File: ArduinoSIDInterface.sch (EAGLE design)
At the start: 25 parts, among them IC1 74HC595N, IC2 74HC595N, T1 BC547

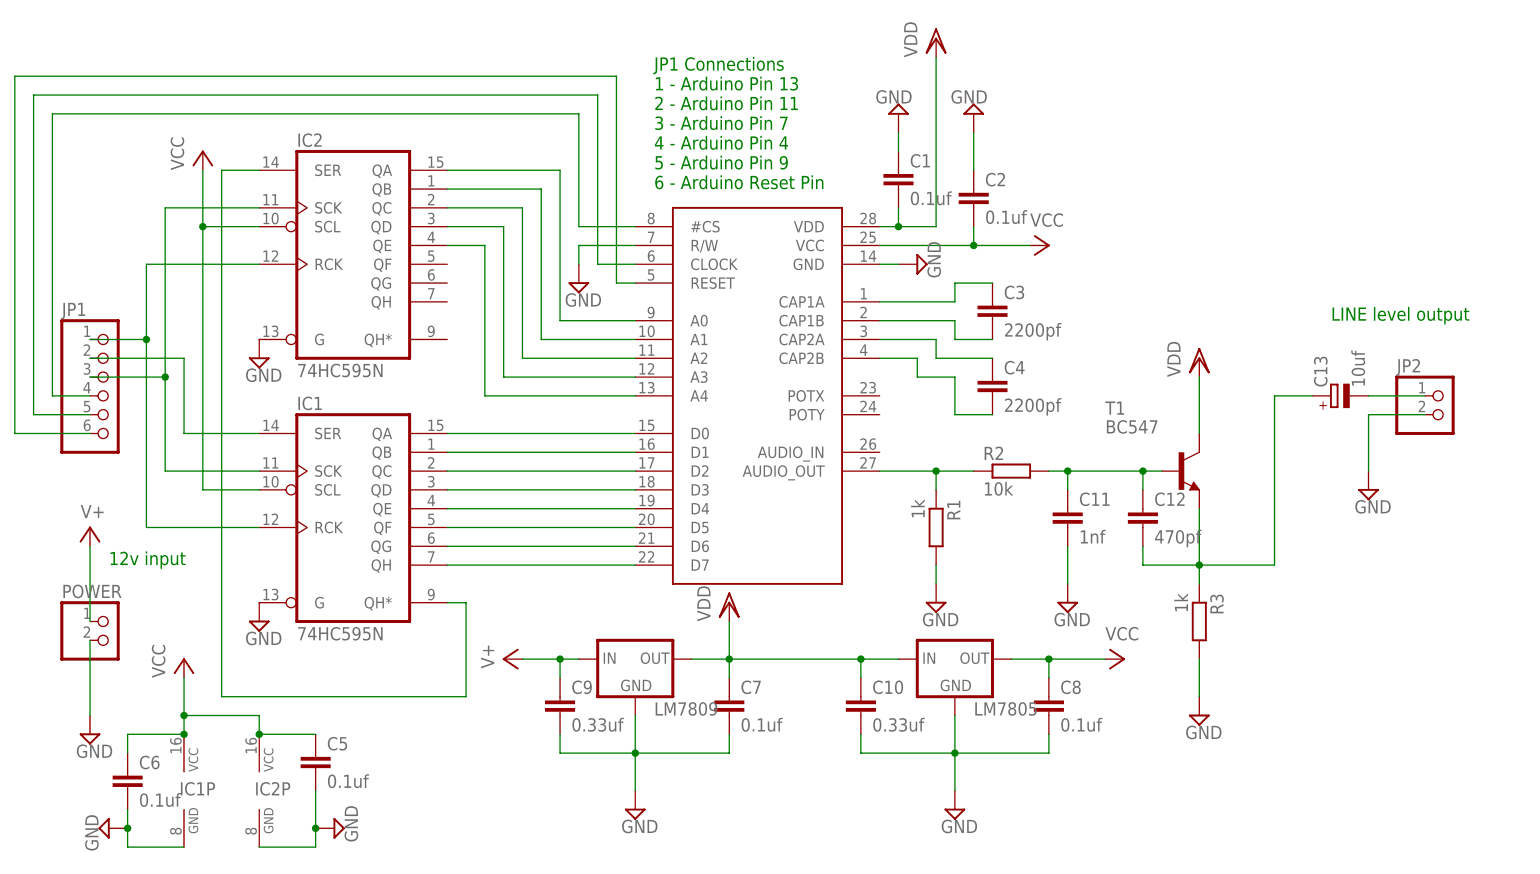
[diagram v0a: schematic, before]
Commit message: Revised the schematic and board layout. Shift register->SID connections now inverted so Q7->D0 and Q0->D7. Requires a change to the SPI initialisation to be compatible but the board layout is a lot neater. Now only a single layer, no extra wires required. Make the power lines a lot thicker - I believe this is the thing to do. Added additional 5v power out header to power external Arduino.
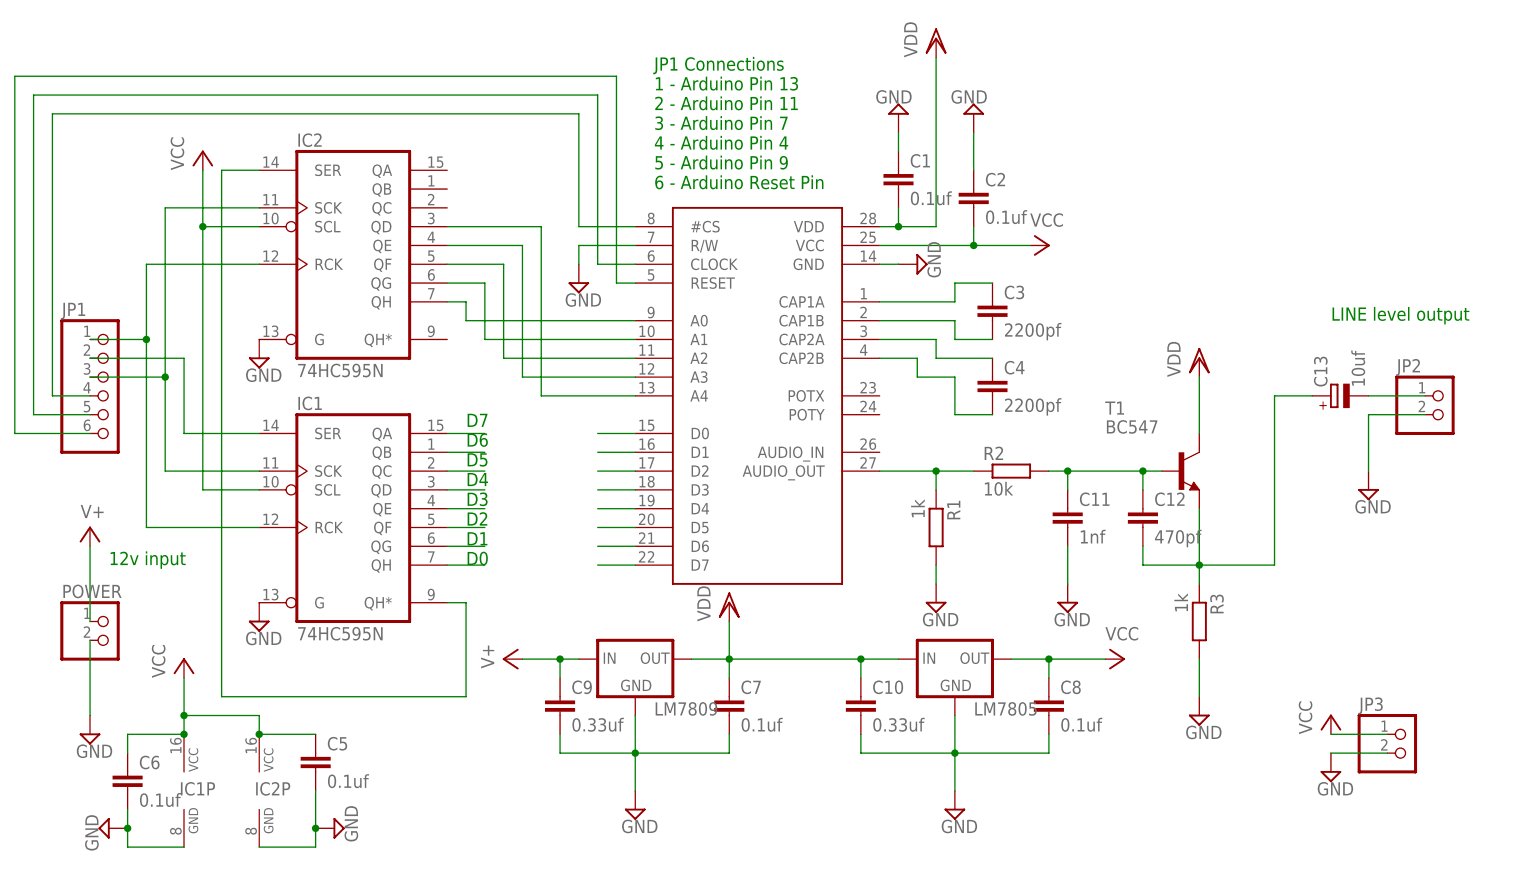
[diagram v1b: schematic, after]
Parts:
- added JP3: (no value), pinhead:PINHD-1X2
- C1: device rcl:C-EU025-030X050 -> rcl:C-EU050-035X075
- C2: device rcl:C-EU025-030X050 -> rcl:C-EU050-030X075
- C3, C4: device rcl:C-EU050-075X075 -> rcl:C-EU075-042X103
- C5, C6: device rcl:C-EU025-025X050 -> rcl:C-EU050-030X075
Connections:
- removed net N$10: IC1A.QB, U$1.D1
- removed net N$13: IC1A.QE, U$1.D4
- removed net N$14: IC1A.QC, U$1.D2
- removed net N$15: IC1A.QD, U$1.D3
- removed net N$18: IC1A.QG, U$1.D6
- removed net N$19: IC1A.QH, U$1.D7
- removed net N$8: IC1A.QF, U$1.D5
- removed net N$9: IC1A.QA, U$1.D0
- new net D0: IC1A.QH, U$1.D0
- new net D1: IC1A.QG, U$1.D1
- new net D2: IC1A.QF, U$1.D2
- new net D3: IC1A.QE, U$1.D3
- new net D4: IC1A.QD, U$1.D4
- new net D5: IC1A.QC, U$1.D5
- new net D6: IC1A.QB, U$1.D6
- new net D7: IC1A.QA, U$1.D7
- net GND: now also JP3.2
- net N$3: now also IC2A.QH; no longer IC2A.QA
- net N$4: now also IC2A.QG; no longer IC2A.QB
- net N$5: now also IC2A.QF; no longer IC2A.QC
- net N$6: now also IC2A.QE; no longer IC2A.QD
- net N$7: now also IC2A.QD; no longer IC2A.QE
- net VCC: now also JP3.1
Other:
- note added: "D7 D6 D5 D4 D3 D2 D1 D0"

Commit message: Fixup schematic
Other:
- note removed: "D7 D6 D5 D4 D3 D2 D1 D0"
- moved on the sheet: IC1
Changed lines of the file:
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@@
 <text x="-25.4" y="27.94" size="1.778" layer="91">12v input</text>
 <text x="139.7" y="60.96" size="1.778" layer="91">LINE level output</text>
-<text x="22.86" y="27.94" size="1.778" layer="91">D7
-D6
-D5
-D4
-D3
-D2
-D1
-D0</text>
 </plain>
 <instances>
 <instance part="U$1" gate="G$1" x="73.66" y="48.26"/>
-<instance part="IC1" gate="A" x="7.62" y="35.56"/>
+<instance part="IC1" gate="A" x="7.62" y="35.56" rot="MR180"/>
 <instance part="IC2" gate="A" x="7.62" y="71.12" smashed="yes">
 <attribute name="NAME" x="0" y="84.455" size="1.778" layer="95" font="vector"/>
@@
 <instance part="C1" gate="G$1" x="81.28" y="81.28"/>
 <instance part="C2" gate="G$1" x="91.44" y="78.74"/>
-<instance part="SUPPLY3" gate="GND" x="-5.08" y="20.32"/>
+<instance part="SUPPLY3" gate="GND" x="-5.08" y="43.18"/>
 <instance part="SUPPLY4" gate="GND" x="-5.08" y="55.88"/>
 <instance part="SUPPLY5" gate="GND" x="81.28" y="88.9" rot="R180"/>
@@
 <segment>
 <pinref part="IC1" gate="A" pin="QH*"/>
-<wire x1="20.32" y1="22.86" x2="22.86" y2="22.86" width="0.1524" layer="91"/>
-<wire x1="22.86" y1="22.86" x2="22.86" y2="10.16" width="0.1524" layer="91"/>
+<wire x1="20.32" y1="48.26" x2="22.86" y2="48.26" width="0.1524" layer="91"/>
+<wire x1="22.86" y1="48.26" x2="22.86" y2="10.16" width="0.1524" layer="91"/>
 <wire x1="22.86" y1="10.16" x2="-10.16" y2="10.16" width="0.1524" layer="91"/>
 <wire x1="-10.16" y1="10.16" x2="-10.16" y2="81.28" width="0.1524" layer="91"/>
@@
 <segment>
 <pinref part="IC1" gate="A" pin="SCK"/>
-<wire x1="-17.78" y1="40.64" x2="-5.08" y2="40.64" width="0.1524" layer="91"/>
+<wire x1="-17.78" y1="30.48" x2="-5.08" y2="30.48" width="0.1524" layer="91"/>
 <pinref part="IC2" gate="A" pin="SCK"/>
-<wire x1="-17.78" y1="40.64" x2="-17.78" y2="53.34" width="0.1524" layer="91"/>
+<wire x1="-17.78" y1="30.48" x2="-17.78" y2="53.34" width="0.1524" layer="91"/>
 <wire x1="-17.78" y1="53.34" x2="-17.78" y2="76.2" width="0.1524" layer="91"/>
 <wire x1="-17.78" y1="76.2" x2="-5.08" y2="76.2" width="0.1524" layer="91"/>
@@
 <wire x1="-20.32" y1="68.58" x2="-5.08" y2="68.58" width="0.1524" layer="91"/>
 <pinref part="IC1" gate="A" pin="RCK"/>
-<wire x1="-5.08" y1="33.02" x2="-20.32" y2="33.02" width="0.1524" layer="91"/>
+<wire x1="-5.08" y1="38.1" x2="-20.32" y2="38.1" width="0.1524" layer="91"/>
 <wire x1="-20.32" y1="68.58" x2="-20.32" y2="58.42" width="0.1524" layer="91"/>
 <pinref part="JP1" gate="A" pin="1"/>
-<wire x1="-20.32" y1="58.42" x2="-20.32" y2="33.02" width="0.1524" layer="91"/>
+<wire x1="-20.32" y1="58.42" x2="-20.32" y2="38.1" width="0.1524" layer="91"/>
 <wire x1="-20.32" y1="58.42" x2="-27.94" y2="58.42" width="0.1524" layer="91"/>
 <junction x="-20.32" y="58.42"/>
@@
 <segment>
 <pinref part="IC1" gate="A" pin="SER"/>
-<wire x1="-15.24" y1="55.88" x2="-15.24" y2="45.72" width="0.1524" layer="91"/>
-<wire x1="-15.24" y1="45.72" x2="-5.08" y2="45.72" width="0.1524" layer="91"/>
+<wire x1="-15.24" y1="55.88" x2="-15.24" y2="25.4" width="0.1524" layer="91"/>
+<wire x1="-15.24" y1="25.4" x2="-5.08" y2="25.4" width="0.1524" layer="91"/>
 <pinref part="JP1" gate="A" pin="2"/>
 <wire x1="-15.24" y1="55.88" x2="-27.94" y2="55.88" width="0.1524" layer="91"/>
@@
 <pinref part="IC1" gate="A" pin="G"/>
 <pinref part="SUPPLY3" gate="GND" pin="GND"/>
+<wire x1="-5.08" y1="48.26" x2="-5.08" y2="45.72" width="0.1524" layer="91"/>
 </segment>
 <segment>
@@
 <pinref part="IC2" gate="A" pin="SCL"/>
 <wire x1="-12.7" y1="73.66" x2="-5.08" y2="73.66" width="0.1524" layer="91"/>
-<wire x1="-12.7" y1="73.66" x2="-12.7" y2="38.1" width="0.1524" layer="91"/>
+<wire x1="-12.7" y1="73.66" x2="-12.7" y2="33.02" width="0.1524" layer="91"/>
 <junction x="-12.7" y="73.66"/>
 <pinref part="IC1" gate="A" pin="SCL"/>
-<wire x1="-12.7" y1="38.1" x2="-5.08" y2="38.1" width="0.1524" layer="91"/>
+<wire x1="-12.7" y1="33.02" x2="-5.08" y2="33.02" width="0.1524" layer="91"/>
 <pinref part="P+1" gate="VCC" pin="VCC"/>
 </segment>
@@
 <segment>
 <pinref part="IC1" gate="A" pin="QB"/>
-<wire x1="20.32" y1="43.18" x2="25.4" y2="43.18" width="0.1524" layer="91"/>
+<wire x1="20.32" y1="27.94" x2="40.64" y2="30.48" width="0.1524" layer="91"/>
 </segment>
 </net>
@@
 <segment>
 <pinref part="IC1" gate="A" pin="QA"/>
-<wire x1="20.32" y1="45.72" x2="25.4" y2="45.72" width="0.1524" layer="91"/>
+<wire x1="20.32" y1="25.4" x2="40.64" y2="27.94" width="0.1524" layer="91"/>
 </segment>
 </net>
@@
 <segment>
 <pinref part="IC1" gate="A" pin="QC"/>
-<wire x1="20.32" y1="40.64" x2="25.4" y2="40.64" width="0.1524" layer="91"/>
+<wire x1="20.32" y1="30.48" x2="40.64" y2="33.02" width="0.1524" layer="91"/>
 </segment>
 <segment>
@@
 <segment>
 <pinref part="IC1" gate="A" pin="QD"/>
-<wire x1="20.32" y1="38.1" x2="25.4" y2="38.1" width="0.1524" layer="91"/>
+<wire x1="20.32" y1="33.02" x2="40.64" y2="35.56" width="0.1524" layer="91"/>
 </segment>
 <segment>
@@
 <segment>
 <pinref part="IC1" gate="A" pin="QE"/>
-<wire x1="20.32" y1="35.56" x2="25.4" y2="35.56" width="0.1524" layer="91"/>
+<wire x1="20.32" y1="35.56" x2="40.64" y2="38.1" width="0.1524" layer="91"/>
 </segment>
 </net>
@@
 <segment>
 <pinref part="IC1" gate="A" pin="QF"/>
-<wire x1="20.32" y1="33.02" x2="25.4" y2="33.02" width="0.1524" layer="91"/>
+<wire x1="20.32" y1="38.1" x2="40.64" y2="40.64" width="0.1524" layer="91"/>
 </segment>
 <segment>
@@
 <segment>
 <pinref part="IC1" gate="A" pin="QG"/>
-<wire x1="20.32" y1="30.48" x2="25.4" y2="30.48" width="0.1524" layer="91"/>
+<wire x1="20.32" y1="40.64" x2="40.64" y2="43.18" width="0.1524" layer="91"/>
 </segment>
 <segment>
@@
 <segment>
 <pinref part="IC1" gate="A" pin="QH"/>
-<wire x1="20.32" y1="27.94" x2="25.4" y2="27.94" width="0.1524" layer="91"/>
-</segment>
-</net>
+<wire x1="20.32" y1="43.18" x2="40.64" y2="45.72" width="0.1524" layer="91"/>
+</segment>
+</net>
